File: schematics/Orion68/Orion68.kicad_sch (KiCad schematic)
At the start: 1 part

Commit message: Updating cpu
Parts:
- gave numbers to parts that had none: 1
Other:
- removed sheet Orion68-CPU
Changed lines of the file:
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@@
 		(dnp no)
 		(fields_autoplaced yes)
-		(property "Reference" "J?"
+		(property "Reference" "J0"
 			(at 254.635 15.24 0)
 			(effects
@@
 			(project "Orion68"
 				(path "/c7ab032b-c937-44de-ab42-c91dee57f0a8"
-					(reference "J?")
+					(reference "J0")
 					(unit 1)
 				)
@@
 		(dnp no)
 		(fields_autoplaced yes)
-		(property "Reference" "#PWR?"
+		(property "Reference" "#PWR02"
 			(at 256.54 105.41 0)
 			(effects
@@
 			(project "Orion68"
 				(path "/c7ab032b-c937-44de-ab42-c91dee57f0a8"
-					(reference "#PWR?")
+					(reference "#PWR02")
 					(unit 1)
 				)
@@
 		(dnp no)
 		(fields_autoplaced yes)
-		(property "Reference" "#PWR?"
+		(property "Reference" "#PWR01"
 			(at 245.11 105.41 0)
 			(effects
@@
 			(project "Orion68"
 				(path "/c7ab032b-c937-44de-ab42-c91dee57f0a8"
-					(reference "#PWR?")
+					(reference "#PWR01")
 					(unit 1)
 				)
@@
 		(dnp no)
 		(fields_autoplaced yes)
-		(property "Reference" "#PWR?"
+		(property "Reference" "#PWR03"
 			(at 266.7 105.41 0)
 			(effects
@@
 			(project "Orion68"
 				(path "/c7ab032b-c937-44de-ab42-c91dee57f0a8"
-					(reference "#PWR?")
+					(reference "#PWR03")
 					(unit 1)
 				)
@@
 				)
 			)
-		)
-	)
-	(sheet
-		(at 20.32 24.13)
-		(size 32.385 15.875)
-		(exclude_from_sim no)
-		(in_bom yes)
-		(on_board yes)
-		(dnp no)
-		(fields_autoplaced yes)
-		(stroke
-			(width 0.1524)
-			(type solid)
-		)
-		(fill
-			(color 0 0 0 0.0000)
-		)
-		(property "Sheetname" "Orion68-CPU"
-			(at 20.32 23.4184 0)
-			(effects
-				(font
-					(size 1.27 1.27)
-				)
-				(justify left bottom)
-			)
-		)
-		(property "Sheetfile" "orion68cpu.kicad_sch"
-			(at 20.32 40.5896 0)
-			(effects
-				(font
-					(size 1.27 1.27)
-				)
-				(justify left top)
-			)
-		)
-		(instances
-			(project "Orion68"
-				(path "/c7ab032b-c937-44de-ab42-c91dee57f0a8"
-					(page "2")
-				)
-			)

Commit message: Schematics update
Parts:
- removed J0: ~, ConnPdSilva:conn_euro96, symbol ConnPdSilva:ConnEuro96

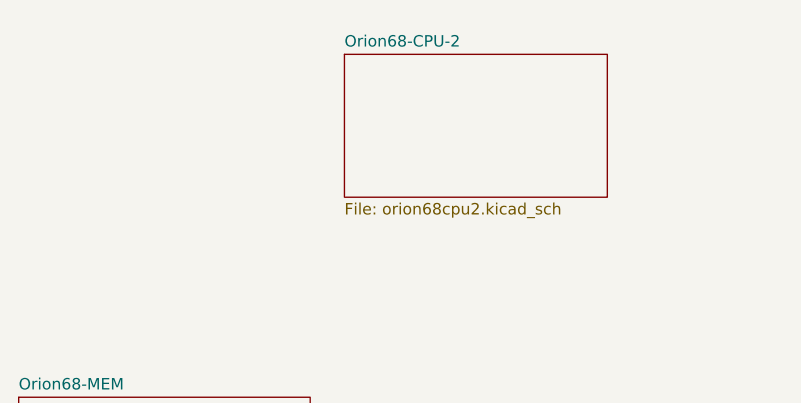
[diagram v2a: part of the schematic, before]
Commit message: Schematic verified to board
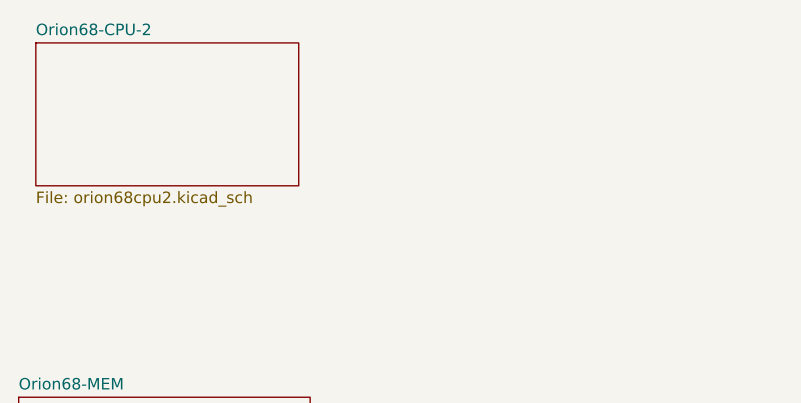
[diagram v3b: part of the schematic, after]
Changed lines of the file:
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@@
 	)
 	(sheet
-		(at 56.515 24.13)
+		(at 22.225 22.86)
 		(size 29.21 15.875)
 		(exclude_from_sim no)
@@
 		)
 		(property "Sheetname" "Orion68-CPU-2"
-			(at 56.515 23.4184 0)
+			(at 22.225 22.1484 0)
 			(effects
 				(font
@@
 		)
 		(property "Sheetfile" "orion68cpu2.kicad_sch"
-			(at 56.515 40.5896 0)
+			(at 22.225 39.3196 0)
 			(effects
 				(font

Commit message: Cpu board fixed and running
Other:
- added sheet cpu2 (cpu2.kicad_sch)
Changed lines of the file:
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@@
+	)
+	(sheet
+		(at 20.32 182.245)
+		(size 32.385 12.7)
+		(exclude_from_sim no)
+		(in_bom yes)
+		(on_board yes)
+		(dnp no)
+		(fields_autoplaced yes)
+		(stroke
+			(width 0.1524)
+			(type solid)
+		)
+		(fill
+			(color 0 0 0 0.0000)
+		)
+		(property "Sheetname" "cpu2"
+			(at 20.32 181.5334 0)
+			(effects
+				(font
+					(size 1.27 1.27)
+				)
+				(justify left bottom)
+			)
+		)
+		(property "Sheetfile" "cpu2.kicad_sch"
+			(at 20.32 195.5296 0)
+			(effects
+				(font
+					(size 1.27 1.27)
+				)
+				(justify left top)
+			)
+		)
+		(instances
+			(project "Orion68"
+				(path "/c7ab032b-c937-44de-ab42-c91dee57f0a8"
+					(page "6")
+				)
+			)
+		)
 	)
 	(sheet

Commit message: Updating...
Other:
- sheet Orion68-CPU-2 renamed Orion68-CPU_cmos
- sheet cpu2 renamed Orion68-CPU_nmos
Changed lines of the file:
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@@
 			(color 0 0 0 0.0000)
 		)
-		(property "Sheetname" "cpu2"
+		(property "Sheetname" "Orion68-CPU_nmos"
 			(at 20.32 181.5334 0)
 			(effects
@@
 			(color 0 0 0 0.0000)
 		)
-		(property "Sheetname" "Orion68-CPU-2"
+		(property "Sheetname" "Orion68-CPU_cmos"
 			(at 22.225 22.1484 0)
 			(effects

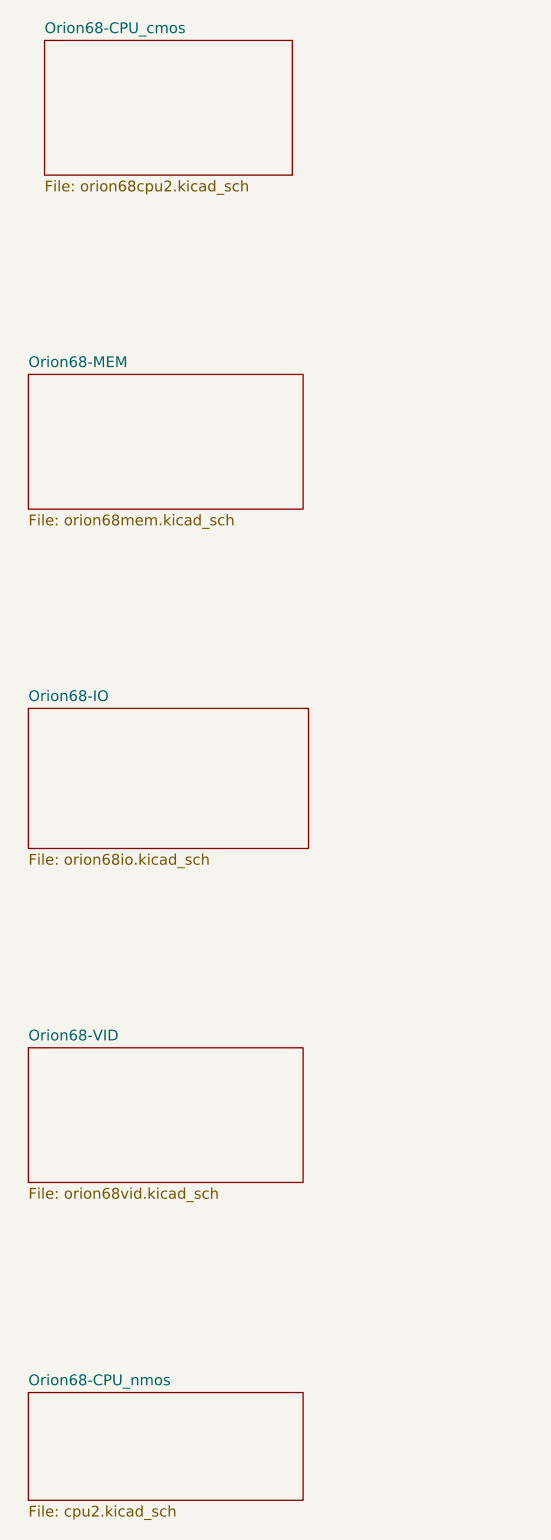
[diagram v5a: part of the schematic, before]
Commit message: A20 bug fixed, missing serial CSA, running ok
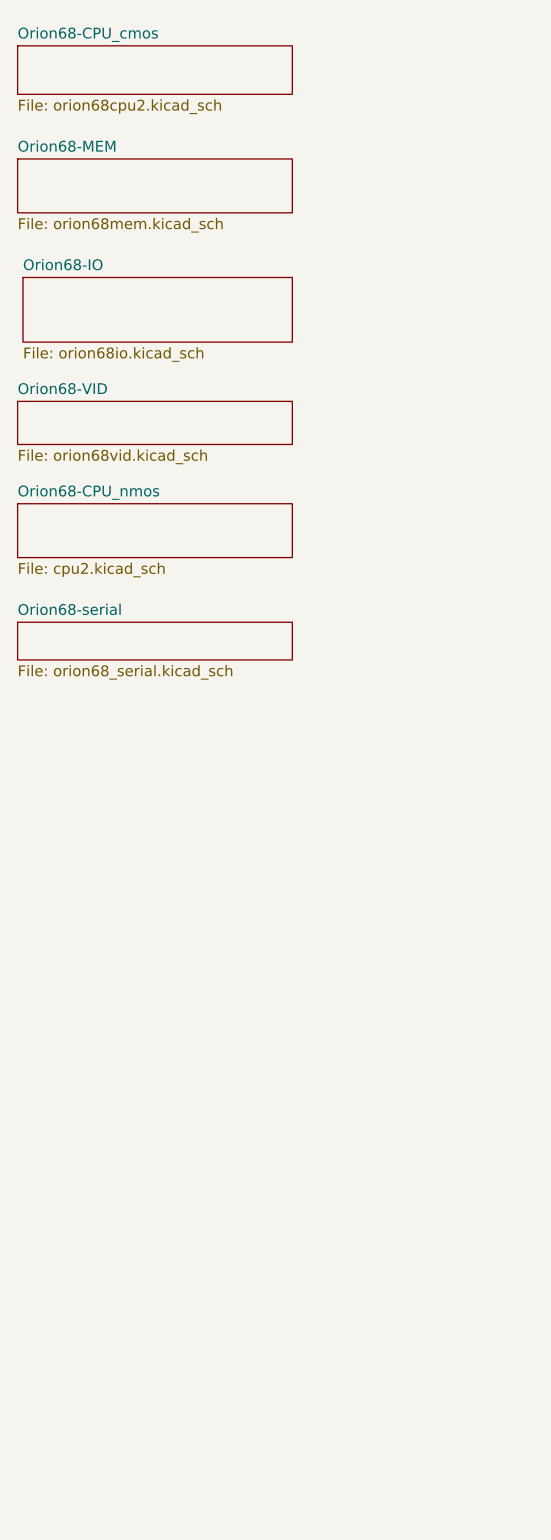
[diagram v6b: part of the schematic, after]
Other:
- added sheet Orion68-serial (orion68_serial.kicad_sch)
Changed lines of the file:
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@@
 	)
 	(sheet
-		(at 20.32 182.245)
-		(size 32.385 12.7)
+		(at 19.05 77.47)
+		(size 32.385 6.35)
 		(exclude_from_sim no)
 		(in_bom yes)
@@
 		)
 		(property "Sheetname" "Orion68-CPU_nmos"
-			(at 20.32 181.5334 0)
+			(at 19.05 76.7584 0)
 			(effects
 				(font
@@
 		)
 		(property "Sheetfile" "cpu2.kicad_sch"
-			(at 20.32 195.5296 0)
+			(at 19.05 84.4046 0)
 			(effects
 				(font
@@
 	)
 	(sheet
-		(at 20.32 141.605)
-		(size 32.385 15.875)
+		(at 19.05 65.405)
+		(size 32.385 5.08)
 		(exclude_from_sim no)
 		(in_bom yes)
@@
 		)
 		(property "Sheetname" "Orion68-VID"
-			(at 20.32 140.8934 0)
+			(at 19.05 64.6934 0)
 			(effects
 				(font
@@
 		)
 		(property "Sheetfile" "orion68vid.kicad_sch"
-			(at 20.32 158.0646 0)
+			(at 19.05 71.0696 0)
 			(effects
 				(font
@@
 	)
 	(sheet
-		(at 20.32 62.23)
-		(size 32.385 15.875)
+		(at 19.05 36.83)
+		(size 32.385 6.35)
 		(exclude_from_sim no)
 		(in_bom yes)
@@
 		)
 		(property "Sheetname" "Orion68-MEM"
-			(at 20.32 61.5184 0)
+			(at 19.05 36.1184 0)
 			(effects
 				(font
@@
 		)
 		(property "Sheetfile" "orion68mem.kicad_sch"
-			(at 20.32 78.6896 0)
+			(at 19.05 43.7646 0)
 			(effects
 				(font
@@
 	)
 	(sheet
-		(at 20.32 101.6)
-		(size 33.02 16.51)
+		(at 19.05 91.44)
+		(size 32.385 4.445)
+		(exclude_from_sim no)
+		(in_bom yes)
+		(on_board yes)
+		(dnp no)
+		(fields_autoplaced yes)
+		(stroke
+			(width 0.1524)
+			(type solid)
+		)
+		(fill
+			(color 0 0 0 0.0000)
+		)
+		(property "Sheetname" "Orion68-serial"
+			(at 19.05 90.7284 0)
+			(effects
+				(font
+					(size 1.27 1.27)
+				)
+				(justify left bottom)
+			)
+		)
+		(property "Sheetfile" "orion68_serial.kicad_sch"
+			(at 19.05 96.4696 0)
+			(effects
+				(font
+					(size 1.27 1.27)
+				)
+				(justify left top)
+			)
+		)
+		(instances
+			(project "Orion68"
+				(path "/c7ab032b-c937-44de-ab42-c91dee57f0a8"
+					(page "7")
+				)
+			)
+		)
+	)
+	(sheet
+		(at 19.685 50.8)
+		(size 31.75 7.62)
 		(exclude_from_sim no)
 		(in_bom yes)
@@
 		)
 		(property "Sheetname" "Orion68-IO"
-			(at 20.32 100.8884 0)
+			(at 19.685 50.0884 0)
 			(effects
 				(font
@@
 		)
 		(property "Sheetfile" "orion68io.kicad_sch"
-			(at 20.32 118.6946 0)
+			(at 19.685 59.0046 0)
 			(effects
 				(font
@@
 	)
 	(sheet
-		(at 22.225 22.86)
-		(size 29.21 15.875)
+		(at 19.05 23.495)
+		(size 32.385 5.715)
 		(exclude_from_sim no)
 		(in_bom yes)
@@
 		)
 		(property "Sheetname" "Orion68-CPU_cmos"
-			(at 22.225 22.1484 0)
+			(at 19.05 22.7834 0)
 			(effects
 				(font
@@
 		)
 		(property "Sheetfile" "orion68cpu2.kicad_sch"
-			(at 22.225 39.3196 0)
-			(effects
-				(font
+			(at 19.05 29.7946 0)
+			(effects
+				(font

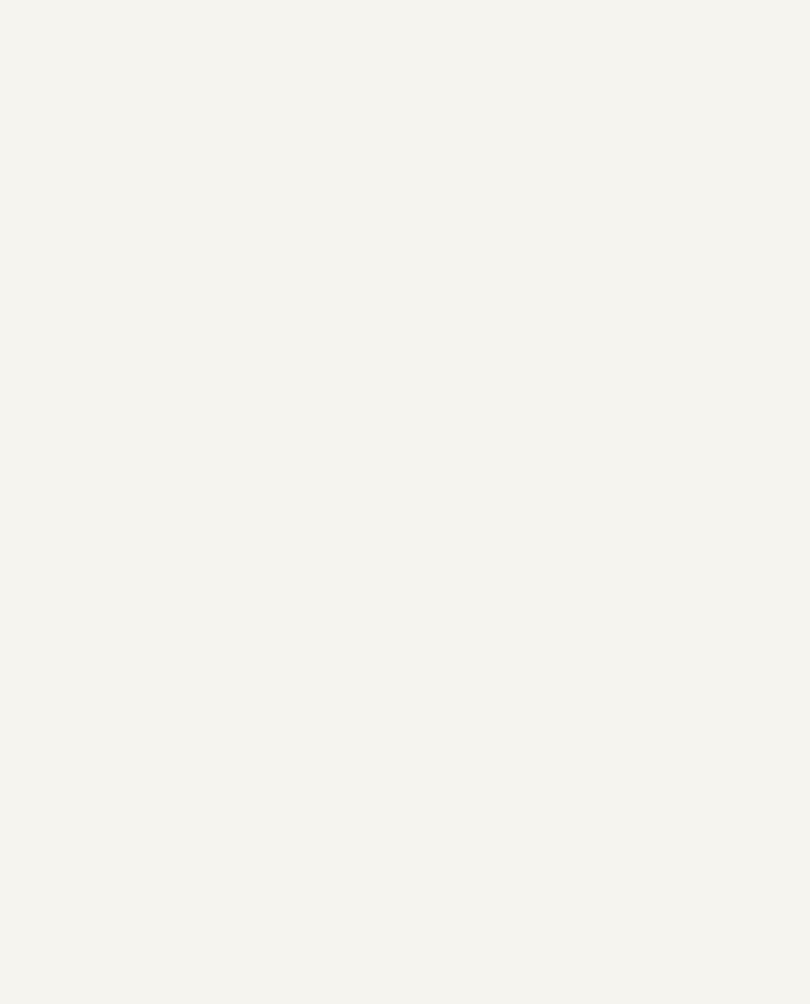
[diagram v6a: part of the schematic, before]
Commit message: B column DIN conn. all in GND
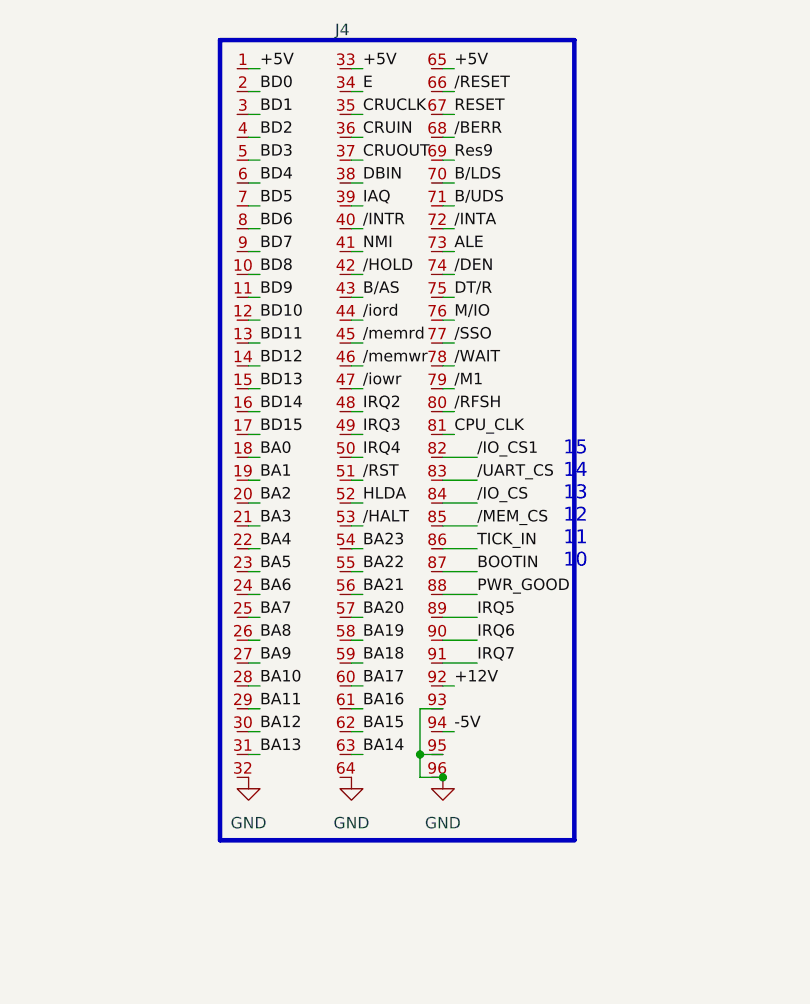
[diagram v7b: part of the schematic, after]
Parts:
- added J4: Euro96pin, ConnPdSilva:conn_euro96, symbol ConnPdSilva:ConnEuro96
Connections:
- new net +12V: J4.92
- new net +5V: J4.1, J4.33, J4.65
- new net -5V: J4.94
- new net ALE: J4.73
- new net BA0: J4.18
- new net BA1: J4.19
- new net BA10: J4.28
- new net BA11: J4.29
- new net BA12: J4.30
- new net BA13: J4.31
- new net BA14: J4.63
- new net BA15: J4.62
- new net BA16: J4.61
- new net BA17: J4.60
- new net BA18: J4.59
- new net BA19: J4.58
- new net BA2: J4.20
- new net BA20: J4.57
- new net BA21: J4.56
- new net BA22: J4.55
- new net BA23: J4.54
- new net BA3: J4.21
- new net BA4: J4.22
- new net BA5: J4.23
- new net BA6: J4.24
- new net BA7: J4.25
- new net BA8: J4.26
- new net BA9: J4.27
- new net BD0: J4.2
- new net BD1: J4.3
- new net BD10: J4.12
- new net BD11: J4.13
- new net BD12: J4.14
- new net BD13: J4.15
- new net BD14: J4.16
- new net BD15: J4.17
- new net BD2: J4.4
- new net BD3: J4.5
- new net BD4: J4.6
- new net BD5: J4.7
- new net BD6: J4.8
- new net BD7: J4.9
- new net BD8: J4.10
- new net BD9: J4.11
- new net BOOTIN: J4.87
- new net B/AS: J4.43
- new net B/LDS: J4.70
- new net B/UDS: J4.71
- new net CPU_CLK: J4.81
- new net CRUCLK: J4.35
- new net CRUIN: J4.36
- new net CRUOUT: J4.37
- new net DBIN: J4.38
- new net DT/R: J4.75
- new net E: J4.34
- new net GND: J4.32, J4.64, J4.93, J4.95, J4.96
- new net HLDA: J4.52
- new net IAQ: J4.39
- new net IRQ2: J4.48
- new net IRQ3: J4.49
- new net IRQ4: J4.50
- new net IRQ5: J4.89
- new net IRQ6: J4.90
- new net IRQ7: J4.91
- new net M/IO: J4.76
- new net NMI: J4.41
- new net PWR_GOOD: J4.88
- new net RESET: J4.67
- new net Res9: J4.69
- new net TICK_IN: J4.86
- new net /BERR: J4.68
- new net /DEN: J4.74
- new net /HALT: J4.53
- new net /HOLD: J4.42
- new net /INTA: J4.72
- new net /INTR: J4.40
- new net /IO_CS: J4.84
- new net /IO_CS1: J4.82
- new net /M1: J4.79
- new net /MEM_CS: J4.85
- new net /RESET: J4.66
- new net /RFSH: J4.80
- new net /RST: J4.51
- new net /SSO: J4.77
- new net /UART_CS: J4.83
- new net /WAIT: J4.78
- new net /iord: J4.44
- new net /iowr: J4.47
- new net /memrd: J4.45
- new net /memwr: J4.46
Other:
- note added: "15 14 13 12 11 10"

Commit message: Implementation drive ide initiated
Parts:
- removed J4: Euro96pin, ConnPdSilva:conn_euro96, symbol ConnPdSilva:ConnEuro96
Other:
- added sheet Ide (ide.kicad_sch)
- note removed: "15 14 13 12 11 10"
